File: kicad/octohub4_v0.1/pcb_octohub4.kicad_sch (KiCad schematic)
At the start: 11 parts, among them J101 USB-231-ARY, J202 Conn_01x5

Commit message: Collecting components
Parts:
- added H201, H202, H203, H204: MountingHole_Pad, 00_project_library:octohub4_mounting_hole, symbol Mechanical:MountingHole_Pad
- added J102, J103, J104: USB-231-ARY, 00_project_library:USB231ARY, symbol 00_project_library:USB-226-BRW
- added J201: Screw_Terminal_01x02, 00_project_library:KF235-2P, symbol Connector:Screw_Terminal_01x02
- added J203: Barrel_Jack_Switch, 00_project_library:BarrelJack_D5.5mm, symbol Connector:Barrel_Jack_Switch
- added U201: TPS259474LRPWR, 00_project_library:TPS259474LRPWR, symbol 00_project_library:TPS259474LRPWR
- J101: footprint 00_project_library:USB226BRW -> 00_project_library:USB231ARY
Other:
- moved on the sheet: J101

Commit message: Collecting components 3
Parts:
- J101, J102, J103, J104: value USB-231-ARY -> USB231ARY; symbol 00_project_library:USB-226-BRW -> 00_project_library:USB231ARY; Datasheet_alt (none) -> https://datasheet.lcsc.com/lcsc/2008111235_XUNPU-USB-226-BR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; JLC C720525 -> C720524; Manufacturer_Part_Number USB-231-ARY -> USB-226-BRW
- J203: symbol Connector:Barrel_Jack_Switch -> Connector:Barrel_Jack_Switch_MountingPin
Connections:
- net GND: now also J201.2 (Pin_2), J203.2, J203.3, J203.MP (MountPin)
- net +5V: now reaches J203.1
- net +5V: now also J201.1 (Pin_1)
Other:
- moved on the sheet: J201

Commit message: tmp
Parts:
- removed D101: white, 00_project_library:LED_0603_1608Metric, symbol 00_project_library:LED WHITE
- removed H201, H202, H203, H204: MountingHole_Pad, 00_project_library:octohub4_mounting_hole, symbol Mechanical:MountingHole_Pad
- removed J201: Screw_Terminal_01x02, 00_project_library:KF235-2P, symbol Connector:Screw_Terminal_01x02
- removed J202: Conn_01x5, 00_project_library:PinSocket_1x5_P2.54mm_Vertical_squarepad_USB, symbol Connector_Generic:Conn_01x05
- removed J203: Barrel_Jack_Switch, 00_project_library:BarrelJack_D5.5mm, symbol Connector:Barrel_Jack_Switch_MountingPin
- removed R101: 2k2, Resistor_SMD:R_0805_2012Metric, symbol Device:R
- removed U201: TPS259474LRPWR, 00_project_library:TPS259474LRPWR, symbol 00_project_library:TPS259474LRPWR
- added NT107, NT108: octoprobe_NetTie_USB_Differential, 00_project_library:octoprobe_NetTie_USB_Differential, symbol 00_project_library:octoprobe_NetTie_USB_Differential
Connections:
- net _USB_INFRA_D+ is gone; now on an unnamed net: NT104.3
- net _USB_INFRA_D- is gone; now on an unnamed net: NT104.1
- net _USB_PROBE_D+ is gone; now on an unnamed net: NT102.3
- net _USB_PROBE_D- is gone; now on an unnamed net: NT102.1
- net GND: now also J101.4 (GND), J101.MH, J102.4 (GND), J102.MH, J103.4 (GND), J103.MH, J104.4 (GND), J104.MH
- net USB Hub Chip/USB_DM1: now also NT101.3; no longer NT103.3
- net USB Hub Chip/USB_DM2: now also NT103.3
- net USB Hub Chip/USB_DM4: now also NT107.3; no longer NT101.3
- net USB Hub Chip/USB_DP1: now also NT101.1; no longer NT103.1
- net USB Hub Chip/USB_DP2: now also NT103.1
- net USB Hub Chip/USB_DP4: now also NT107.1; no longer NT101.1
- net USB_DUT_D+: now also NT107.2, NT108.4
- net USB_DUT_D-: now also NT107.4, NT108.2
- net at NT106.1: now also J103.2 (D-)
- net at NT106.3: now also J103.3 (D+)
- net +5VOUT: now reaches J104.1 (VBUS)
- net +5VOUT: now also J101.1 (VBUS), J102.1 (VBUS), J103.1 (VBUS)
- net at J104.2 (D-): now also NT108.1
- net at J104.3 (D+): now also NT108.3
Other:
- added sheet Power Protection (pcb_octohub4_usbhubchip_power_protection.kicad_sch)
- note removed: "Port 1: Infra - RP2"
- note removed: "Port 2: Infra - RP2 BOOT"
- note removed: "Port 3: DUT"
- note removed: "Port 4: Probe - RP2"
- note removed: "USB DUT"
- moved on the sheet: J101, J102, J103, J104, NT101, NT102, NT103, NT104, NT105, NT106

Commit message: Add run_kicad_purge 2
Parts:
- added D203, D204, D205, D206: PRTR5V0U2X, Package_SON:Texas_USON-6_1x1.45mm_P0.5mm_SMD, symbol 00_project_library:PRTR5V0U2X
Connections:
- net GND: now also D203.2 (GND), D204.2 (GND), D205.2 (GND), D206.2 (GND)
- net at J101.2 (D-), NT102.1: now also D203.3 (I/O2), D203.4 (I/O2)
- net at J101.3 (D+), NT102.3: now also D203.1 (I/O1), D203.6 (I/O1)
- net at J104.2 (D-), NT108.1: now also D206.3 (I/O2), D206.4 (I/O2)
- net at J104.3 (D+), NT108.3: now also D206.1 (I/O1), D206.6 (I/O1)
- net at J103.2 (D-), NT106.1: now also D205.3 (I/O2), D205.4 (I/O2)
- net at J103.3 (D+), NT106.3: now also D205.1 (I/O1), D205.6 (I/O1)
- net at J102.2 (D-), NT104.1: now also D204.3 (I/O2), D204.4 (I/O2)
- net at J102.3 (D+), NT104.3: now also D204.1 (I/O1), D204.6 (I/O1)
- net +5VOUT renamed +5VPROTECTED
- net +5VPROTECTED: now also D203.5 (VCC), D204.5 (VCC), D205.5 (VCC), D206.5 (VCC)
- net USB_DUT_D+ renamed USB_3_D+
- net USB_3_D+: no longer NT107.2, NT108.4
- net USB_DUT_D- renamed USB_3_D-
- net USB_3_D-: no longer NT107.4, NT108.2
- net USB_INFRA_D+ renamed USB_2_D+
- net USB_INFRA_D- renamed USB_2_D-
- net USB_PROBE_D+ renamed USB_1_D+
- net USB_PROBE_D- renamed USB_1_D-
- new net USB_4_D+: NT107.2, NT108.4
- new net USB_4_D-: NT107.4, NT108.2
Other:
- moved on the sheet: J101, J102, J103, J104, NT101, NT102, NT103, NT104, NT105, NT106, NT107, NT108

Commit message: Add run_kicad_purge 5
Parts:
- J101, J102, J103, J104: JLC C720524 -> C720525
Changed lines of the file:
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@@
 			)
 		)
-		(property "JLC" "C720524"
+		(property "JLC" "C720525"
 			(at 163.83 849.86 0)
 			(effects
@@
 			)
 		)
-		(property "JLC" "C720524"
+		(property "JLC" "C720525"
 			(at 162.56 809.22 0)
 			(effects
@@
 			)
 		)
-		(property "JLC" "C720524"
+		(property "JLC" "C720525"
 			(at 162.56 729.21 0)
 			(effects
@@
 			)
 		)
-		(property "JLC" "C720524"
+		(property "JLC" "C720525"
 			(at 162.56 769.85 0)
 			(effects

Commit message: Add run_kicad_purge 8
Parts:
- J101, J102, J103, J104: Datasheet_alt https://datasheet.lcsc.com/lcsc/2008111235_XUNPU-USB-226-BR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 -> https://jlcpcb.com/api/file/downloadByFileSystemAccessId/86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
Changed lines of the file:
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@@
 			)
 		)
-		(property "Description" "19.414.67.1mm USB Connectors ROHS 4 pin USB 2.0 DC 30V 1.5 A"
+		(property "Description" "USB Connectors ROHS 4 pin USB 2.0 DC 30V 1.5 A"
 			(at 139.7 154.94 0)
 			(effects
@@
 			)
 		)
-		(property "Datasheet_alt" "https://datasheet.lcsc.com/lcsc/2008111235_XUNPU-USB-226-BRW_C720524.pdf"
+		(property "Datasheet_alt" "https://jlcpcb.com/api/file/downloadByFileSystemAccessId/8608741080523153408"
 			(at 139.7 154.94 0)
 			(effects
@@
 			)
 		)
-		(property "Description" "19.414.67.1mm USB Connectors ROHS 4 pin USB 2.0 DC 30V 1.5 A"
+		(property "Description" "USB Connectors ROHS 4 pin USB 2.0 DC 30V 1.5 A"
 			(at 138.43 114.3 0)
 			(effects
@@
 			)
 		)
-		(property "Datasheet_alt" "https://datasheet.lcsc.com/lcsc/2008111235_XUNPU-USB-226-BRW_C720524.pdf"
+		(property "Datasheet_alt" "https://jlcpcb.com/api/file/downloadByFileSystemAccessId/8608741080523153408"
 			(at 138.43 114.3 0)
 			(effects
@@
 			)
 		)
-		(property "Description" "19.414.67.1mm USB Connectors ROHS 4 pin USB 2.0 DC 30V 1.5 A"
+		(property "Description" "USB Connectors ROHS 4 pin USB 2.0 DC 30V 1.5 A"
 			(at 138.43 34.29 0)
 			(effects
@@
 			)
 		)
-		(property "Datasheet_alt" "https://datasheet.lcsc.com/lcsc/2008111235_XUNPU-USB-226-BRW_C720524.pdf"
+		(property "Datasheet_alt" "https://jlcpcb.com/api/file/downloadByFileSystemAccessId/8608741080523153408"
 			(at 138.43 34.29 0)
 			(effects
@@
 			)
 		)
-		(property "Description" "19.414.67.1mm USB Connectors ROHS 4 pin USB 2.0 DC 30V 1.5 A"
+		(property "Description" "USB Connectors ROHS 4 pin USB 2.0 DC 30V 1.5 A"
 			(at 138.43 74.93 0)
 			(effects
@@
 			)
 		)
-		(property "Datasheet_alt" "https://datasheet.lcsc.com/lcsc/2008111235_XUNPU-USB-226-BRW_C720524.pdf"
+		(property "Datasheet_alt" "https://jlcpcb.com/api/file/downloadByFileSystemAccessId/8608741080523153408"
 			(at 138.43 74.93 0)
 			(effects

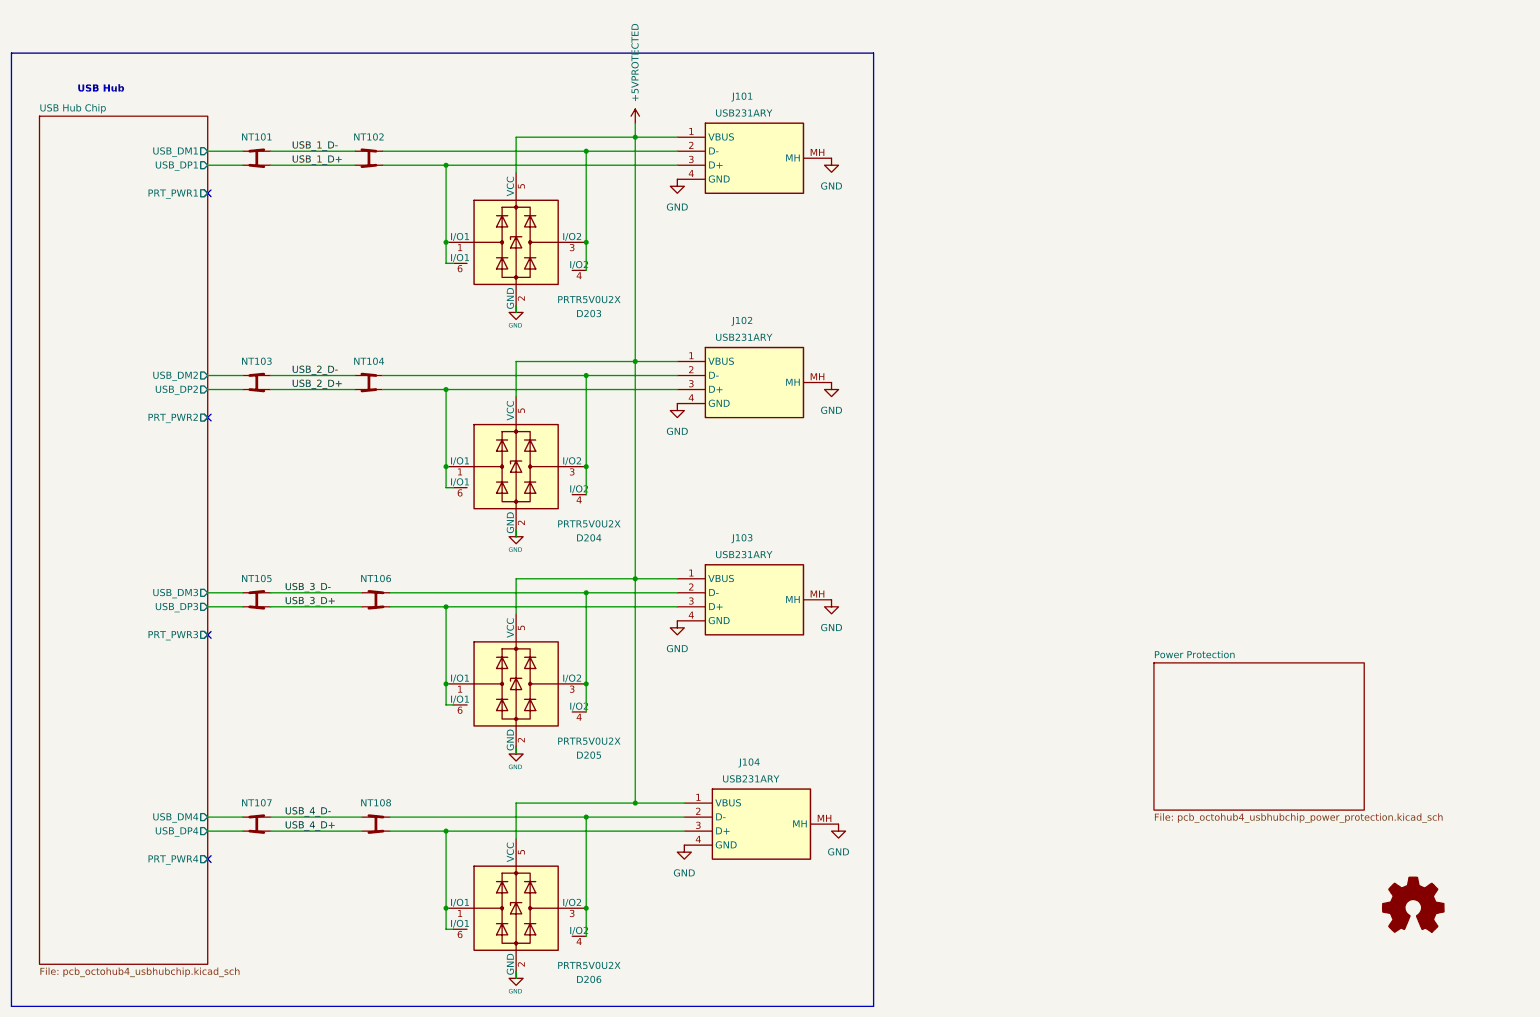
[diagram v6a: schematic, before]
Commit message: Add run_kicad_purge 9
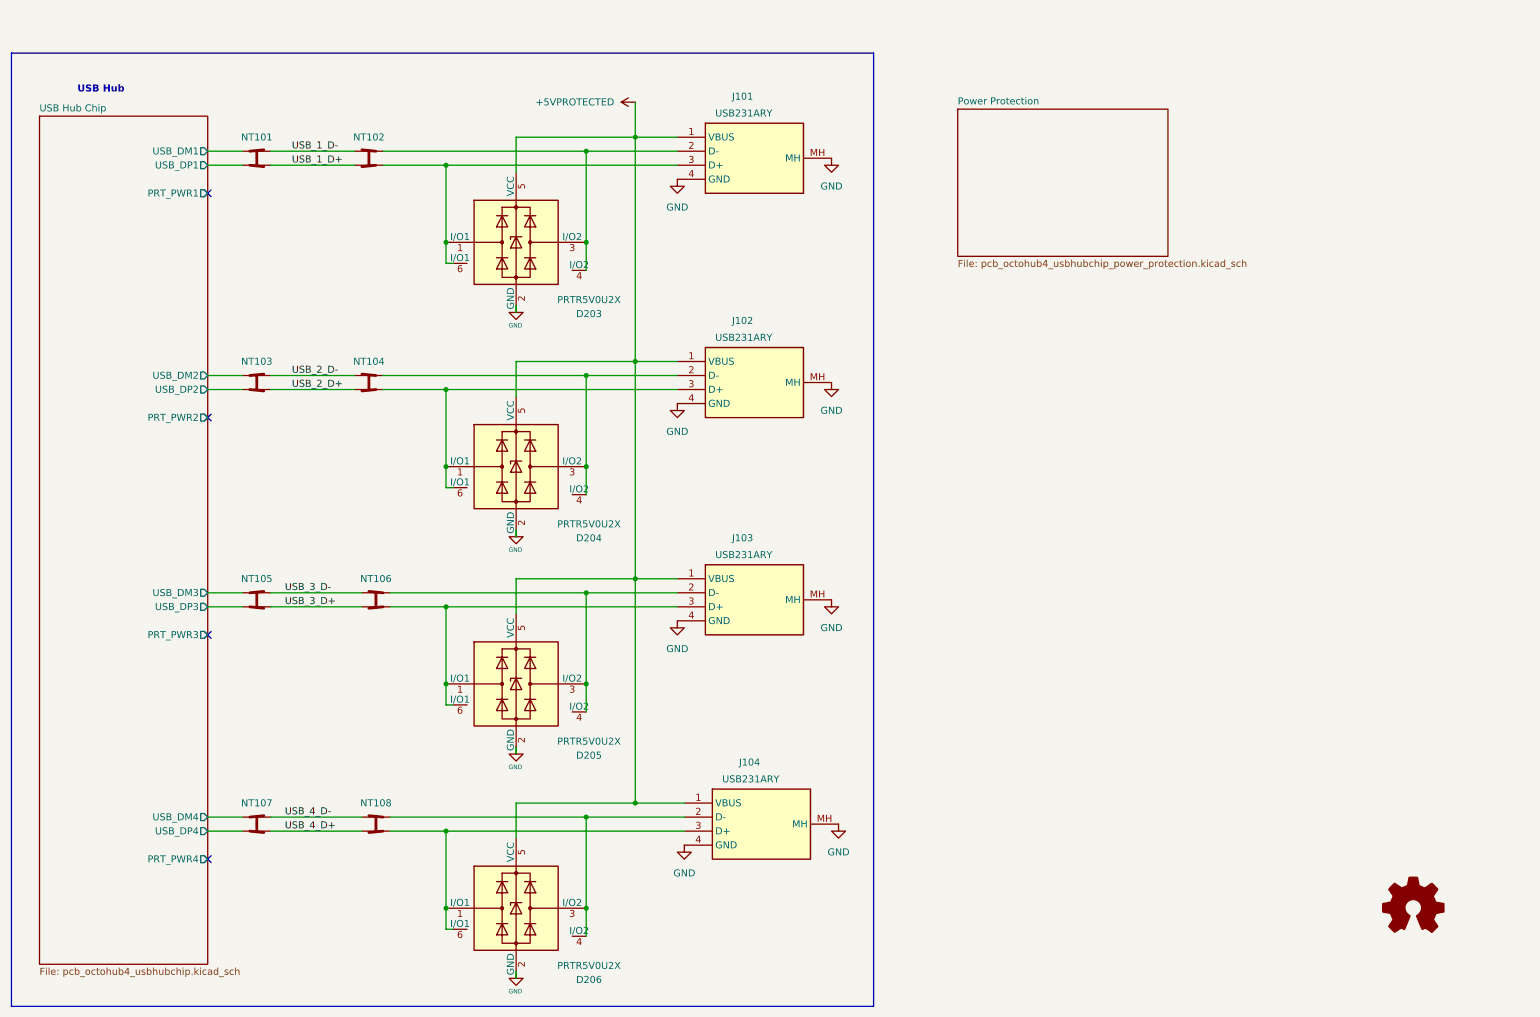
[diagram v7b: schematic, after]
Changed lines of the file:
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@@
 	(title_block
 		(title "Octohub4")
-		(date "2026-01-11")
+		(date "2026-01-20")
 		(rev "0.1")
 		(company "Hans Märki, Märki Informatik")
@@
 	(wire
 		(pts
-			(xy 130.81 31.75) (xy 130.81 34.29)
+			(xy 130.81 27.94) (xy 130.81 34.29)
 		)
 		(stroke
@@
 	(symbol
 		(lib_id "00_project_library:+5VPROTECTED")
-		(at 130.81 31.75 0)
+		(at 130.81 27.94 90)
 		(unit 1)
 		(exclude_from_sim no)
@@
 		(dnp no)
 		(property "Reference" "#PWR0215"
-			(at 130.81 35.56 0)
+			(at 134.62 27.94 0)
 			(effects
 				(font
@@
 		)
 		(property "Value" "+5VPROTECTED"
-			(at 130.8099 27.94 90)
+			(at 127 27.9401 90)
 			(effects
 				(font
@@
 		)
 		(property "Footprint" ""
-			(at 130.81 31.75 0)
+			(at 130.81 27.94 0)
 			(effects
 				(font
@@
 		)
 		(property "Datasheet" ""
-			(at 130.81 31.75 0)
+			(at 130.81 27.94 0)
 			(effects
 				(font
@@
 		)
 		(property "Description" ""
-			(at 130.81 31.75 0)
+			(at 130.81 27.94 0)
 			(effects
 				(font
@@
 	)
 	(sheet
-		(at 224.79 129.54)
+		(at 189.23 29.21)
 		(size 38.1 26.67)
 		(exclude_from_sim no)
@@
 		)
 		(property "Sheetname" "Power Protection"
-			(at 224.79 128.8284 0)
+			(at 189.23 28.4984 0)
 			(effects
 				(font
@@
 		)
 		(property "Sheetfile" "pcb_octohub4_usbhubchip_power_protection.kicad_sch"
-			(at 224.79 156.7946 0)
+			(at 189.23 56.4646 0)
 			(effects
 				(font
